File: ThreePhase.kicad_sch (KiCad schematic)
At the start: 0 parts

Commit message: 增加部分接口
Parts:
- added Q1, Q2, Q3, Q4, Q5, Q6: NMOS, symbol Simulation_SPICE:NMOS
- added R15, R16, R17: R_Small_US, symbol Device:R_Small_US
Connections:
- new net: Q1.3 (S), Q2.1 (D)
- new net: R15.2, R16.2, R17.2
- new net: Q3.3 (S), Q4.1 (D)
- new net: Q5.3 (S), Q6.1 (D)
- new net M0_UH: Q1.2 (G)
- new net M0_UL: Q2.2 (G)
- new net M0_U_CURR: Q2.3 (S), R15.1
- new net M0_VH: Q3.2 (G)
- new net M0_VL: Q4.2 (G)
- new net M0_V_CURR: Q4.3 (S), R16.1
- new net M0_WH: Q5.2 (G)
- new net M0_WL: Q6.2 (G)
- new net M0_W_CURR: Q6.3 (S), R17.1

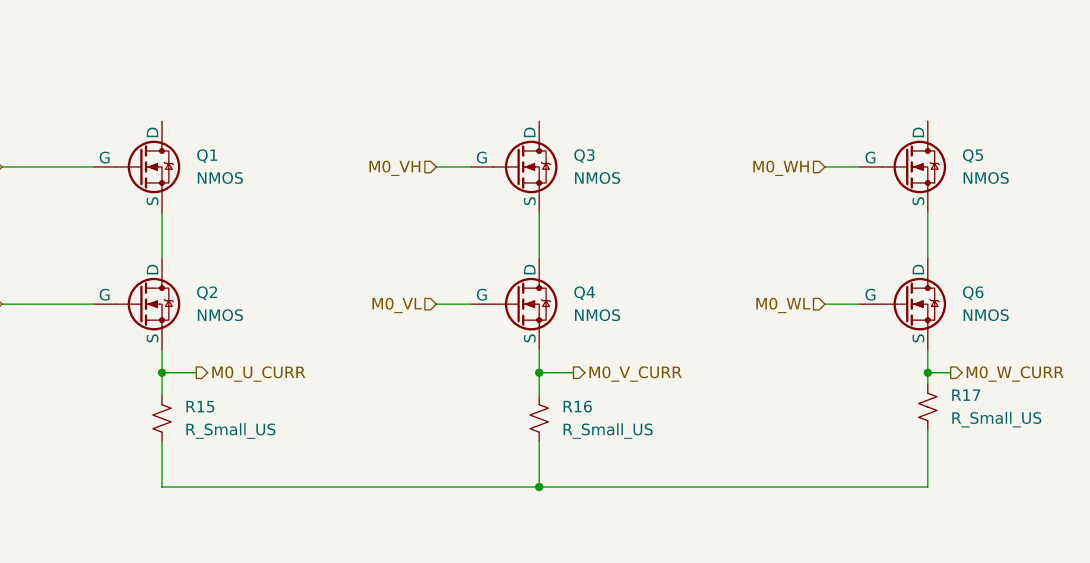
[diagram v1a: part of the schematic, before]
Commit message: 增加预驱/三相桥电路
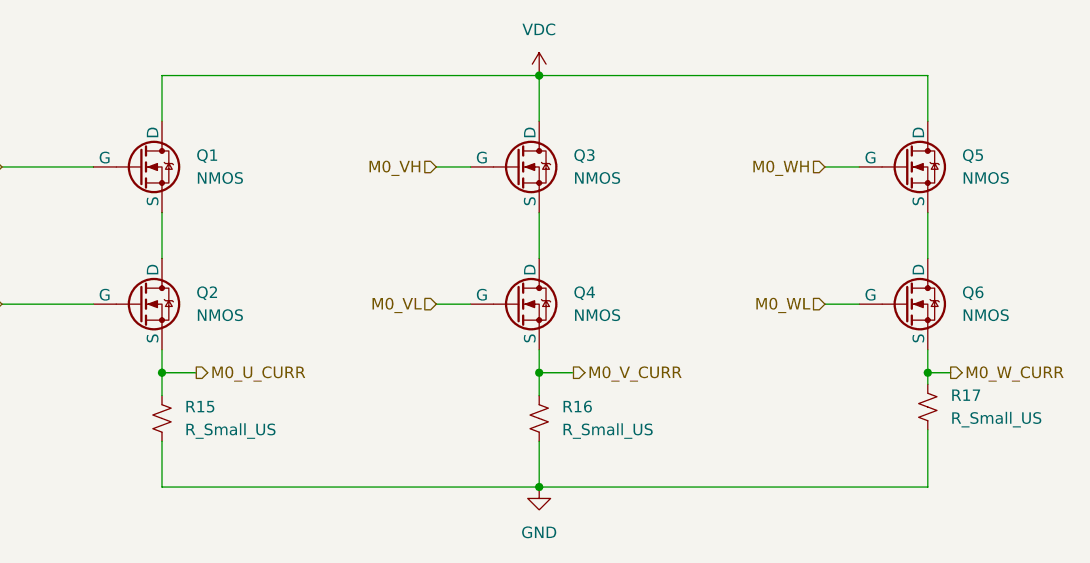
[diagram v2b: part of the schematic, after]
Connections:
- net VDC: now reaches Q1.1 (D)
- net VDC: now also Q3.1 (D), Q5.1 (D)
- net GND: now reaches R15.2, R16.2, R17.2
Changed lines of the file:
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@@
+	)
+	(junction
+		(at 128.27 35.56)
+		(diameter 0)
+		(color 0 0 0 0)
 	)
 	(junction
@@
 	(wire
 		(pts
+			(xy 86.36 40.64) (xy 86.36 35.56)
+		)
+		(stroke
+			(width 0)
+			(type default)
+		)
+	)
+	(wire
+		(pts
+			(xy 128.27 35.56) (xy 171.45 35.56)
+		)
+		(stroke
+			(width 0)
+			(type default)
+		)
+	)
+	(wire
+		(pts
 			(xy 116.84 45.72) (xy 120.65 45.72)
 		)
@@
 	(wire
 		(pts
+			(xy 86.36 35.56) (xy 128.27 35.56)
+		)
+		(stroke
+			(width 0)
+			(type default)
+		)
+	)
+	(wire
+		(pts
 			(xy 128.27 68.58) (xy 128.27 71.12)
 		)
@@
 	(wire
 		(pts
+			(xy 128.27 35.56) (xy 128.27 40.64)
+		)
+		(stroke
+			(width 0)
+			(type default)
+		)
+	)
+	(wire
+		(pts
 			(xy 160.02 45.72) (xy 163.83 45.72)
 		)
@@
 		(pts
 			(xy 160.02 60.96) (xy 163.83 60.96)
+		)
+		(stroke
+			(width 0)
+			(type default)
+		)
+	)
+	(wire
+		(pts
+			(xy 171.45 35.56) (xy 171.45 40.64)
 		)
 		(stroke
@@
 			)
 			(justify right)
+		)
+	)
+	(symbol
+		(lib_id "power:VDC")
+		(at 128.27 35.56 0)
+		(unit 1)
+		(exclude_from_sim no)
+		(in_bom yes)
+		(on_board yes)
+		(dnp no)
+		(fields_autoplaced yes)
+		(property "Reference" "#PWR018"
+			(at 128.27 39.37 0)
+			(effects
+				(font
+					(size 1.27 1.27)
+				)
+				(hide yes)
+			)
+		)
+		(property "Value" "VDC"
+			(at 128.27 30.48 0)
+			(effects
+				(font
+					(size 1.27 1.27)
+				)
+			)
+		)
+		(property "Footprint" ""
+			(at 128.27 35.56 0)
+			(effects
+				(font
+					(size 1.27 1.27)
+				)
+				(hide yes)
+			)
+		)
+		(property "Datasheet" ""
+			(at 128.27 35.56 0)
+			(effects
+				(font
+					(size 1.27 1.27)
+				)
+				(hide yes)
+			)
+		)
+		(property "Description" "Power symbol creates a global label with name \"VDC\""
+			(at 128.27 35.56 0)
+			(effects
+				(font
+					(size 1.27 1.27)
+				)
+				(hide yes)
+			)
+		)
+		(pin "1"
+		)
+		(instances
+			(project ""
+				(path "/6b2aea6d-5084-4a15-abee-69a455b7078c/5772d040-df17-4bf9-89d6-199efe0c04cd"
+					(reference "#PWR018")
+					(unit 1)
+				)
+			)
 		)
 	)
@@
 					(unit 1)
 				)
+			)
+		)
+	)
+	(symbol
+		(lib_id "power:GND")
+		(at 128.27 81.28 0)
+		(unit 1)
+		(exclude_from_sim no)
+		(in_bom yes)
+		(on_board yes)
+		(dnp no)
+		(fields_autoplaced yes)
+		(property "Reference" "#PWR019"
+			(at 128.27 87.63 0)
+			(effects
+				(font
+					(size 1.27 1.27)
+				)
+				(hide yes)
+			)
+		)
+		(property "Value" "GND"
+			(at 128.27 86.36 0)
+			(effects
+				(font
+					(size 1.27 1.27)
+				)
+			)
+		)
+		(property "Footprint" ""
+			(at 128.27 81.28 0)
+			(effects
+				(font
+					(size 1.27 1.27)
+				)
+				(hide yes)
+			)
+		)
+		(property "Datasheet" ""
+			(at 128.27 81.28 0)
+			(effects
+				(font
+					(size 1.27 1.27)
+				)
+				(hide yes)
+			)
+		)
+		(property "Description" "Power symbol creates a global label with name \"GND\" , ground"
+			(at 128.27 81.28 0)
+			(effects
+				(font
+					(size 1.27 1.27)
+				)
+				(hide yes)
+			)
+		)
+		(pin "1"
+		)
+		(instances
+			(project ""
+				(path "/6b2aea6d-5084-4a15-abee-69a455b7078c/5772d040-df17-4bf9-89d6-199efe0c04cd"
+					(reference "#PWR019")
+					(unit 1)
+				)

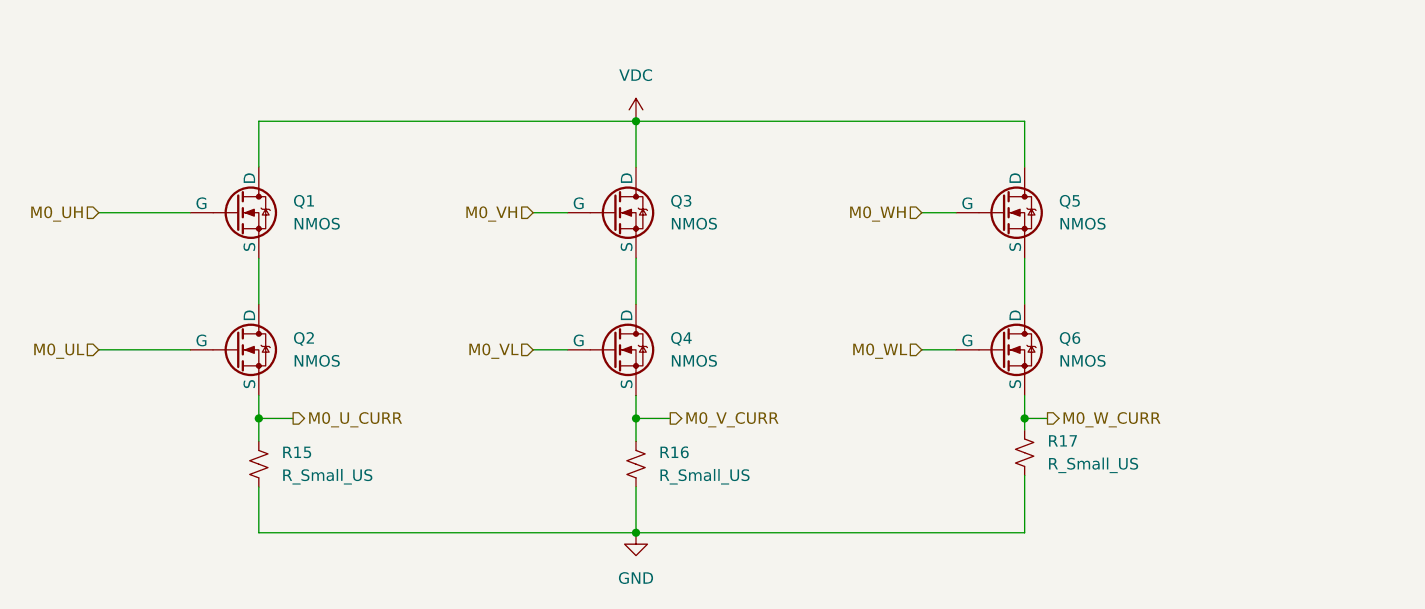
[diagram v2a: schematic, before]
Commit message: 优化5V电源/预驱电路/三相桥/运放
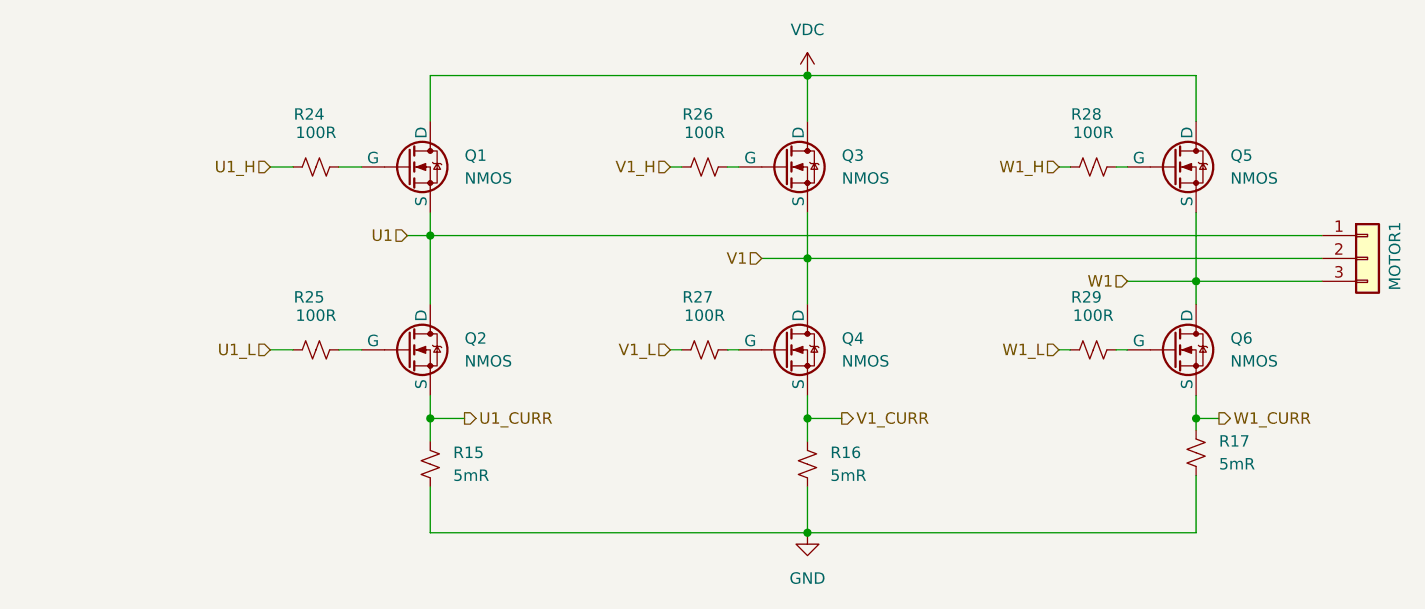
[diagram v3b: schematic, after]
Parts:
- added MOTOR1: Conn_01x03, symbol Connector_Generic:Conn_01x03
- added R24, R25, R26, R27, R28, R29: 100R, symbol Device:R_Small_US
- R15, R16, R17: value R_Small_US -> 5mR
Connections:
- net U1: now reaches Q1.3 (S), Q2.1 (D)
- net U1: now also MOTOR1.1 (Pin_1)
- net V1: now reaches Q3.3 (S), Q4.1 (D)
- net V1: now also MOTOR1.2 (Pin_2)
- net W1: now reaches Q5.3 (S), Q6.1 (D)
- net W1: now also MOTOR1.3 (Pin_3)
- net M0_UH: no longer names the net of Q1.2 (G)
- net M0_UH: now also R24.2
- net M0_UL: no longer names the net of Q2.2 (G)
- net M0_UL: now also R25.2
- net M0_U_CURR renamed U1_CURR
- net M0_VH: no longer names the net of Q3.2 (G)
- net M0_VH: now also R26.2
- net M0_VL: no longer names the net of Q4.2 (G)
- net M0_VL: now also R27.2
- net M0_V_CURR renamed V1_CURR
- net M0_WH: no longer names the net of Q5.2 (G)
- net M0_WH: now also R28.2
- net M0_WL: no longer names the net of Q6.2 (G)
- net M0_WL: now also R29.2
- net M0_W_CURR renamed W1_CURR
- new net U1_H: R24.1
- new net U1_L: R25.1
- new net V1_H: R26.1
- new net V1_L: R27.1
- new net W1_H: R28.1
- new net W1_L: R29.1
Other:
- moved on the sheet: Q1, Q2, Q3, Q4, Q5, Q6, R15, R16, R17

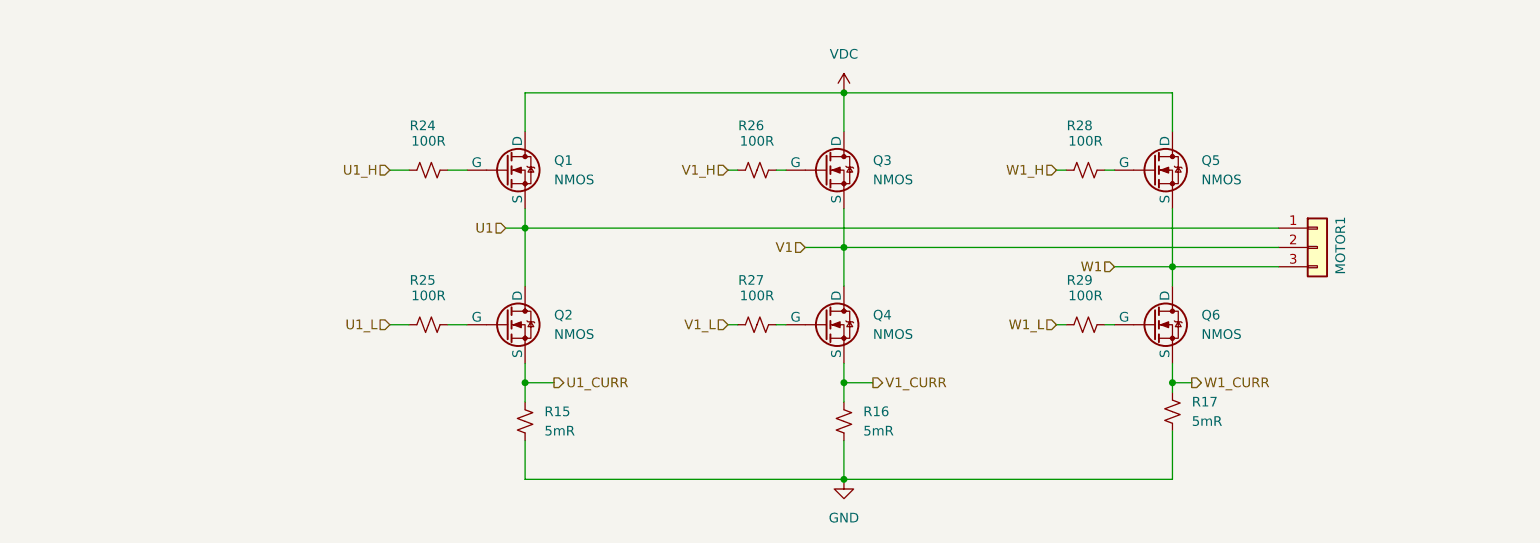
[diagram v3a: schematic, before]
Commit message: 分配部分封装
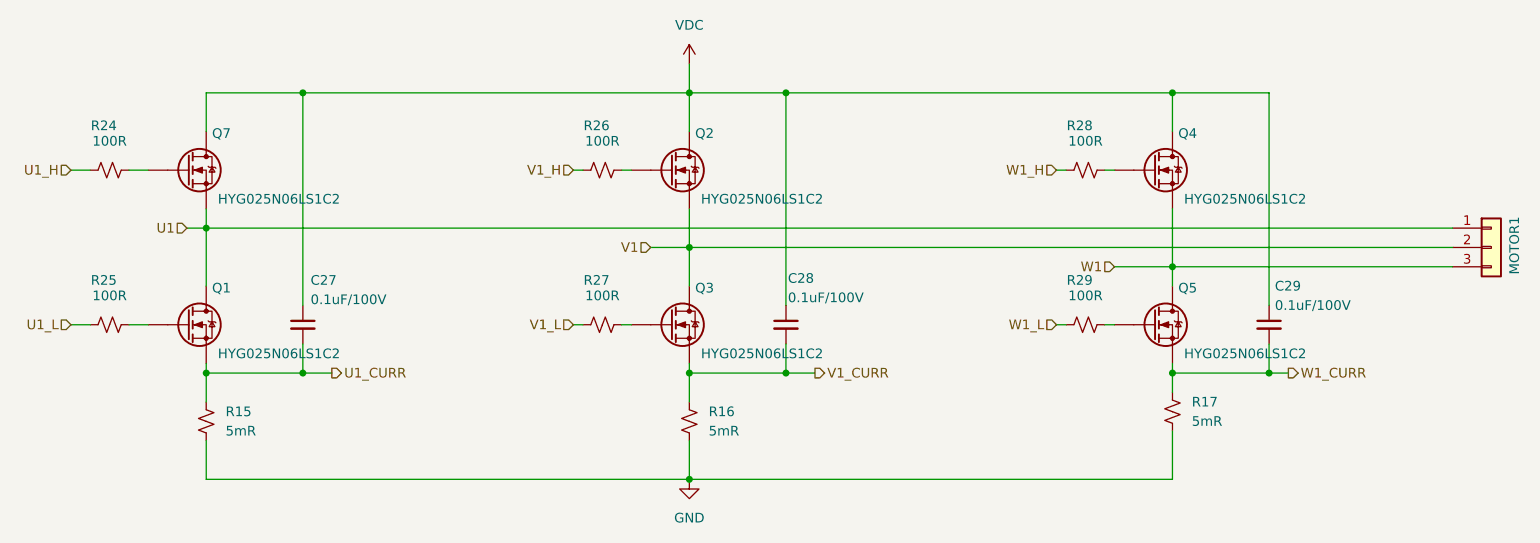
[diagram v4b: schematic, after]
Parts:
- removed Q1, Q2, Q3, Q4, Q5, Q6: NMOS, symbol Simulation_SPICE:NMOS
- added C27, C28, C29: 0.1uF/100V, symbol Device:C_Small
- added Q1, Q2, Q3, Q4, Q5, Q7: HYG025N06LS1C2, Package_DFN_QFN:DFN-8-1EP_6x5mm_P1.27mm_EP4x4mm, symbol User_Driver:HYG025N06
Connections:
- net U1: now also Q1.5 (D), Q7.1 (S)
- net U1_CURR: now also C27.2, Q1.1 (S)
- net V1: now also Q2.1 (S), Q3.5 (D)
- net V1_CURR: now also C28.2, Q3.1 (S)
- net VDC: now also C27.1, C28.1, C29.1, Q2.5 (D), Q4.5 (D), Q7.5 (D)
- net W1: now also Q4.1 (S), Q5.5 (D)
- net W1_CURR: now also C29.2, Q5.1 (S)
- net at R24.2: now also Q7.4 (G)
- net at R28.2: now also Q4.4 (G)
- net at R26.2: now also Q2.4 (G)
- net at R27.2: now also Q3.4 (G)
- net at R25.2: now also Q1.4 (G)
- net at R29.2: now also Q5.4 (G)
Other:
- moved on the sheet: MOTOR1, R15, R16, R24, R25, R26, R27

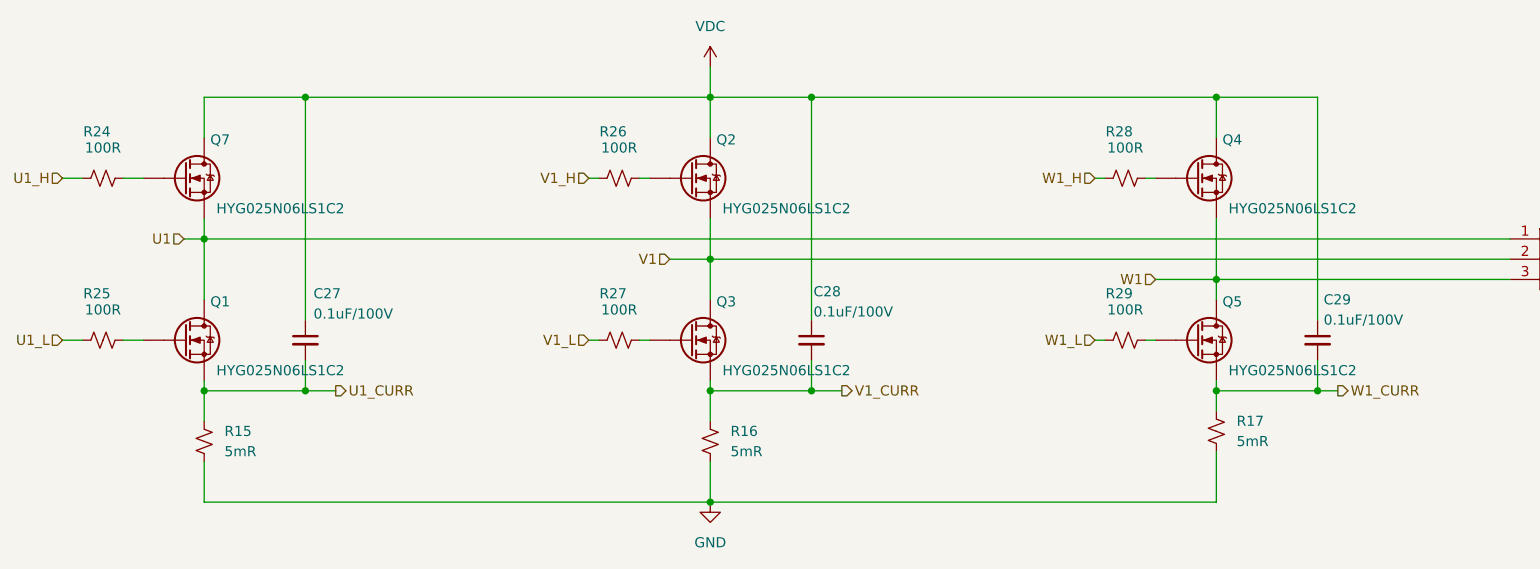
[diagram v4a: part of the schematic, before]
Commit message: 生成网表并添加到PCB
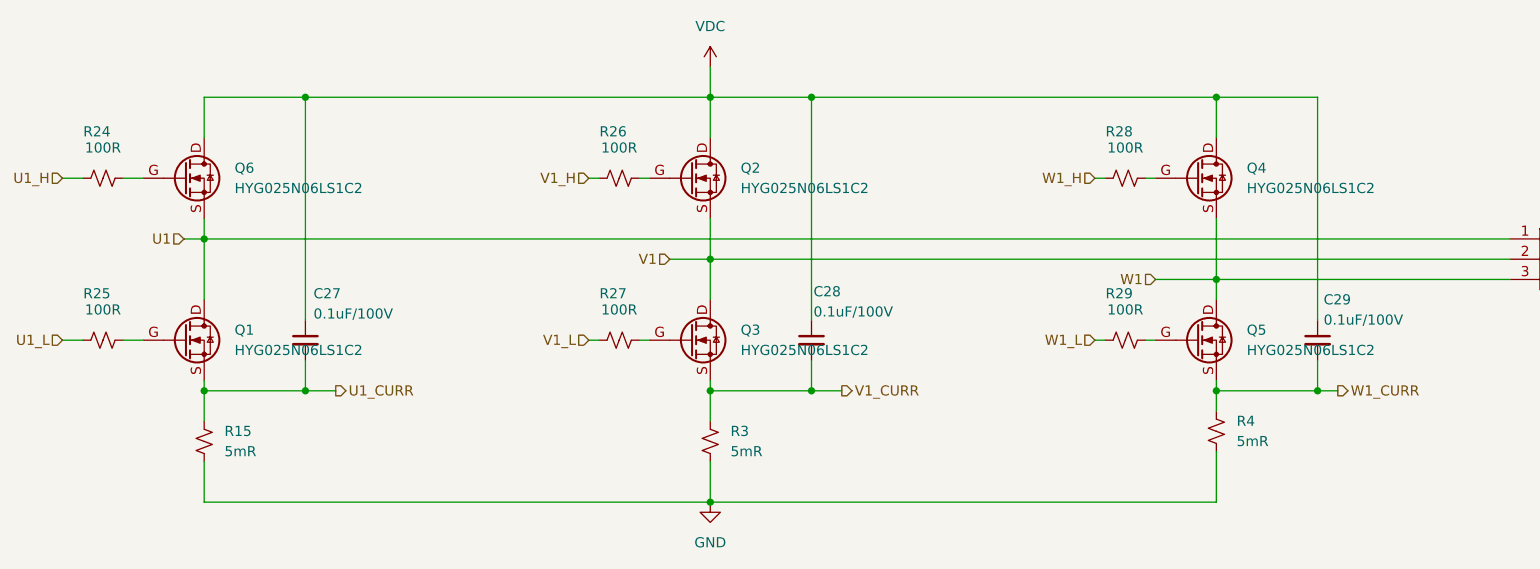
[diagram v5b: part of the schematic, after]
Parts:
- removed Q1, Q2, Q3, Q4, Q5, Q7: HYG025N06LS1C2, Package_DFN_QFN:DFN-8-1EP_6x5mm_P1.27mm_EP4x4mm, symbol User_Driver:HYG025N06
- removed R16, R17: 5mR, symbol Device:R_Small_US
- added Q1, Q2, Q3, Q4, Q5, Q6: HYG025N06LS1C2, footprints:HYG025N06LS1C2-PDFN-8-1EP_6x5mm_P1.27mm_EP3x3mm, symbol User_Driver:NMOS_GDS
- added R3, R4: 5mR, Resistor_SMD:R_1206_3216Metric_Pad1.30x1.75mm_HandSolder, symbol Device:R_Small_US
- C27, C28, C29: footprint (none) -> Capacitor_SMD:C_0603_1608Metric
- MOTOR1: footprint (none) -> footprints:MR30PW-FB_1x03_P3.50mm_Horizontal
- R15: footprint (none) -> Resistor_SMD:R_1206_3216Metric_Pad1.30x1.75mm_HandSolder
- R24, R25, R26, R27, R28, R29: footprint (none) -> Resistor_SMD:R_0603_1608Metric
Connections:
- net GND: now also R3.2, R4.2
- net U1: now also Q1.D, Q6.S
- net U1_CURR: now also Q1.S
- net V1: now also Q2.S, Q3.D
- net V1_CURR: now also Q3.S, R3.1
- net VDC: now also Q2.D, Q4.D, Q6.D
- net W1: now also Q4.S, Q5.D
- net W1_CURR: now also Q5.S, R4.1
- net at R25.2: now also Q1.G
- net at R28.2: now also Q4.G
- net at R24.2: now also Q6.G
- net at R29.2: now also Q5.G
- net at R26.2: now also Q2.G
- net at R27.2: now also Q3.G
